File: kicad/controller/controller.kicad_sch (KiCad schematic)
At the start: 40 parts, among them J1 JST_BAT, J2 JST_BOOKMARK, J3 CONN_UPDI, J4 UART_DBG, Q1 DMP1045U, SW1 SW_DIP_x01, U1 DS3231, U2 TP4056, U3 ATTINY1616

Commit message: fix: fix wrong UPDI & DBG pin label
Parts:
- U4: value ~ -> (none)

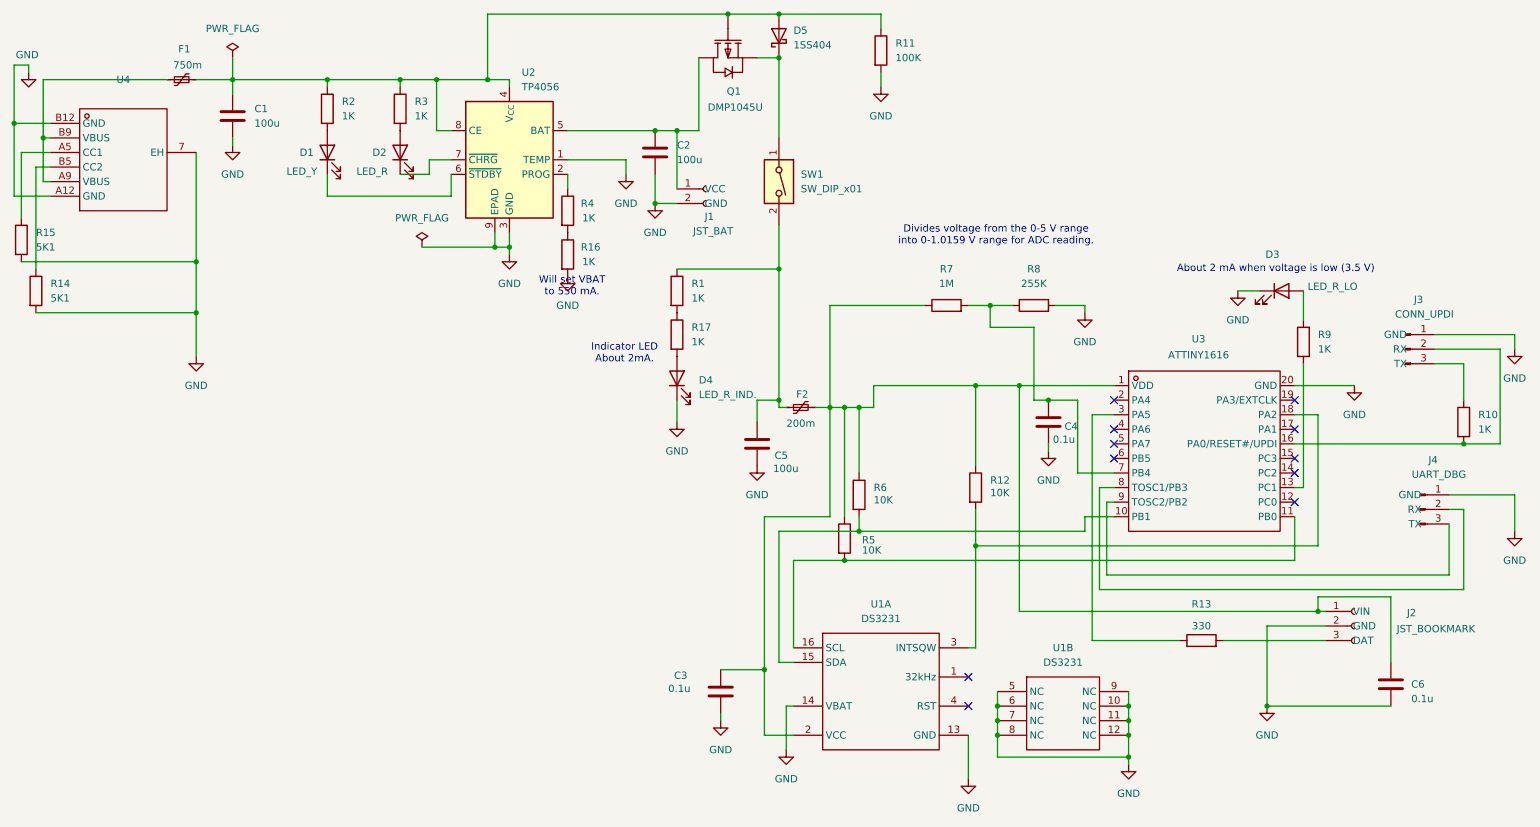
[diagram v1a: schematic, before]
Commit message: fix: make sense of the connection from power to peripherals make the DS3231 get power directly without a switch and add testing pads to connect power to MCU & LEDs in order to measure current.
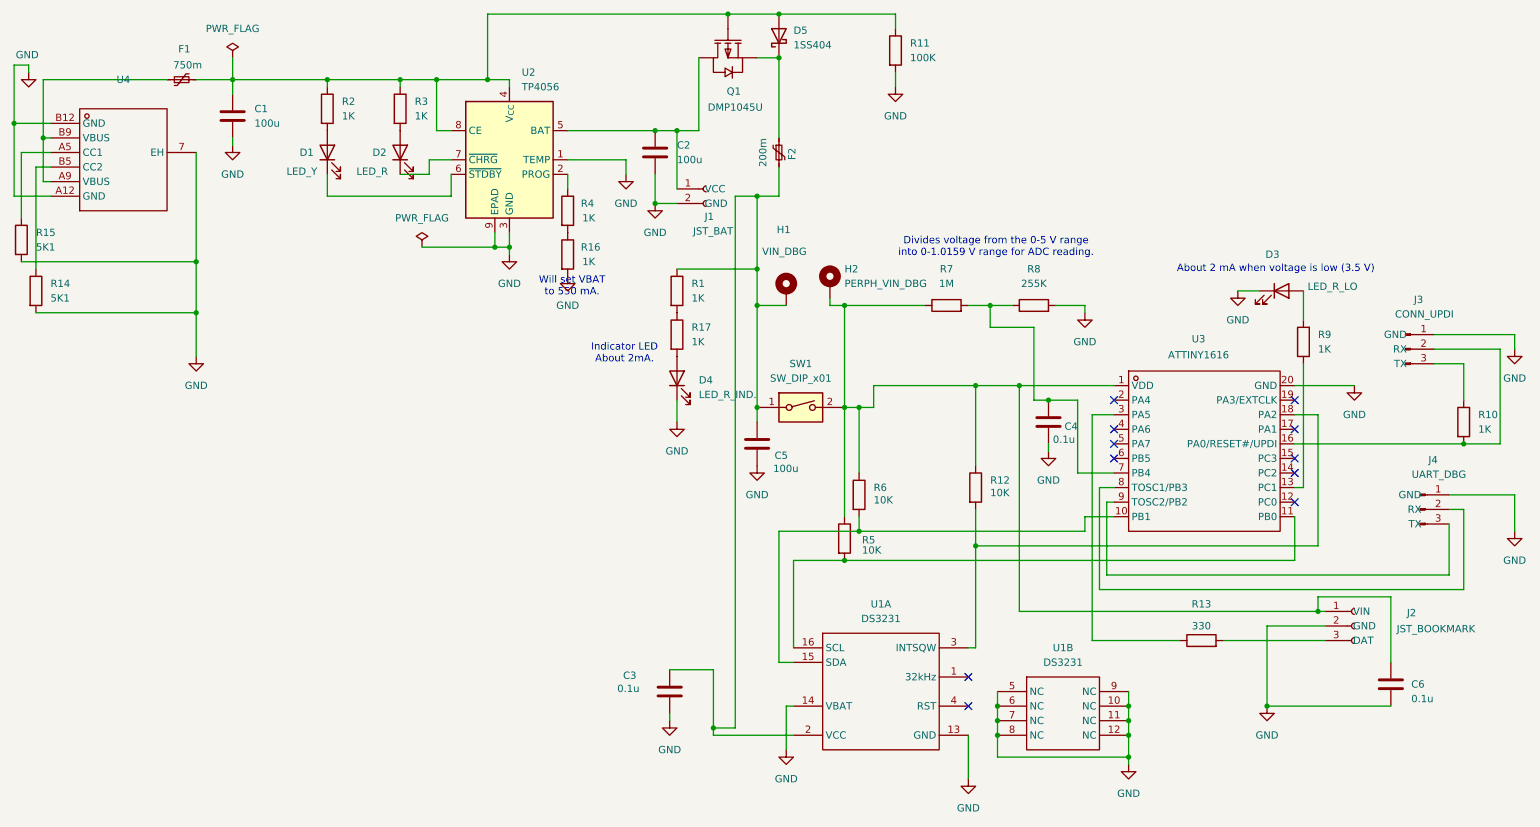
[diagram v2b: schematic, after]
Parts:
- added H1: VIN_DBG, Connector_Wire:SolderWirePad_1x01_SMD_1x2mm, symbol Mechanical:MountingHole_Pad
- added H2: PERPH_VIN_DBG, Connector_Wire:SolderWirePad_1x01_SMD_1x2mm, symbol Mechanical:MountingHole_Pad
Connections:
- net at C6.1, J2.1 (VIN), R12.1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: now also SW1.2, H2.1; no longer C3.1, F2.2, U1.2 (VCC)
- net at C5.1, R1.1: now also C3.1, F2.2, SW1.1, U1.2 (VCC), H1.1; no longer F2.1, SW1.2
- net at D5.1 (K), Q1.2 (S): now also F2.1; no longer SW1.1
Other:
- moved on the sheet: C3, F2, R11, SW1

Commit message: clean up position of footprints
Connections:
- net at C6.1, H2.1, J2.1 (VIN)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: now also R1.1
- net at C3.1, C5.1, F2.2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: no longer R1.1
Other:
- moved on the sheet: D4, R1, R17
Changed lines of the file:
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@@
 	(text "Indicator LED\nAbout 2mA."
 		(exclude_from_sim no)
-		(at 121.666 80.772 0)
+		(at 114.808 92.71 0)
 		(effects
 			(font
@@
 	)
 	(junction
-		(at 144.78 66.04)
-		(diameter 0)
-		(color 0 0 0 0)
-	)
-	(junction
 		(at 53.34 33.02)
 		(diameter 0)
@@
 	)
 	(junction
+		(at 160.02 80.01)
+		(diameter 0)
+		(color 0 0 0 0)
+	)
+	(junction
 		(at 144.78 90.17)
 		(diameter 0)
@@
 	(wire
 		(pts
+			(xy 123.19 80.01) (xy 123.19 83.82)
+		)
+		(stroke
+			(width 0)
+			(type default)
+		)
+	)
+	(wire
+		(pts
 			(xy 186.69 151.13) (xy 209.55 151.13)
 		)
@@
 	(wire
 		(pts
-			(xy 200.66 101.6) (xy 207.01 101.6)
+			(xy 160.02 80.01) (xy 160.02 90.17)
 		)
 		(stroke
@@
 	(wire
 		(pts
-			(xy 201.93 72.39) (xy 201.93 73.66)
+			(xy 200.66 101.6) (xy 207.01 101.6)
 		)
 		(stroke
@@
 	(wire
 		(pts
-			(xy 130.81 66.04) (xy 144.78 66.04)
+			(xy 201.93 72.39) (xy 201.93 73.66)
 		)
 		(stroke
@@
 	(wire
 		(pts
-			(xy 144.78 66.04) (xy 144.78 72.39)
+			(xy 144.78 53.34) (xy 144.78 72.39)
 		)
 		(stroke
@@
 	(wire
 		(pts
-			(xy 144.78 53.34) (xy 144.78 66.04)
-		)
-		(stroke
-			(width 0)
-			(type default)
-		)
-	)
-	(wire
-		(pts
 			(xy 17.78 30.48) (xy 17.78 31.75)
 		)
@@
 	(wire
 		(pts
-			(xy 130.81 88.9) (xy 130.81 92.71)
+			(xy 123.19 106.68) (xy 123.19 110.49)
 		)
 		(stroke
@@
 	(wire
 		(pts
+			(xy 160.02 80.01) (xy 123.19 80.01)
+		)
+		(stroke
+			(width 0)
+			(type default)
+		)
+	)
+	(wire
+		(pts
 			(xy 15.24 40.64) (xy 15.24 53.34)
 		)
@@
 	(wire
 		(pts
-			(xy 160.02 72.39) (xy 160.02 90.17)
+			(xy 160.02 72.39) (xy 160.02 80.01)
 		)
 		(stroke
@@
 	(symbol
 		(lib_id "Device:LED")
-		(at 130.81 85.09 90)
+		(at 123.19 102.87 90)
 		(unit 1)
 		(body_style 1)
@@
 		(fields_autoplaced yes)
 		(property "Reference" "D4"
-			(at 134.62 85.4074 90)
+			(at 127 103.1874 90)
 			(show_name no)
 			(do_not_autoplace no)
@@
 		)
 		(property "Value" "LED_R_IND."
-			(at 134.62 87.9474 90)
+			(at 127 105.7274 90)
 			(show_name no)
 			(do_not_autoplace no)
@@
 		)
 		(property "Footprint" "LED_THT:LED_D2.0mm_W4.8mm_H2.5mm_FlatTop"
-			(at 130.81 85.09 0)
+			(at 123.19 102.87 0)
 			(hide yes)
 			(show_name no)
@@
 		)
 		(property "Datasheet" ""
-			(at 130.81 85.09 0)
+			(at 123.19 102.87 0)
 			(hide yes)
 			(show_name no)
@@
 		)
 		(property "Description" "Light emitting diode"
-			(at 130.81 85.09 0)
+			(at 123.19 102.87 0)
 			(hide yes)
 			(show_name no)
@@
 		)
 		(property "Sim.Pins" "1=K 2=A"
-			(at 130.81 85.09 0)
+			(at 123.19 102.87 0)
 			(hide yes)
 			(show_name no)
@@
 	(symbol
 		(lib_id "Device:R")
-		(at 130.81 69.85 0)
+		(at 123.19 87.63 0)
 		(unit 1)
 		(body_style 1)
@@
 		(fields_autoplaced yes)
 		(property "Reference" "R1"
-			(at 133.35 68.5799 0)
+			(at 125.73 86.3599 0)
 			(show_name no)
 			(do_not_autoplace no)
@@
 		)
 		(property "Value" "1K"
-			(at 133.35 71.1199 0)
+			(at 125.73 88.8999 0)
 			(show_name no)
 			(do_not_autoplace no)
@@
 		)
 		(property "Footprint" "Resistor_SMD:R_0603_1608Metric"
-			(at 129.032 69.85 90)
+			(at 121.412 87.63 90)
 			(hide yes)
 			(show_name no)
@@
 		)
 		(property "Datasheet" ""
-			(at 130.81 69.85 0)
+			(at 123.19 87.63 0)
 			(hide yes)
 			(show_name no)
@@
 		)
 		(property "Description" "Resistor"
-			(at 130.81 69.85 0)
+			(at 123.19 87.63 0)
 			(hide yes)
 			(show_name no)
@@
 	(symbol
 		(lib_id "Device:R")
-		(at 130.81 77.47 0)
+		(at 123.19 95.25 0)
 		(unit 1)
 		(body_style 1)
@@
 		(fields_autoplaced yes)
 		(property "Reference" "R17"
-			(at 133.35 76.1999 0)
+			(at 125.73 93.9799 0)
 			(show_name no)
 			(do_not_autoplace no)
@@
 		)
 		(property "Value" "1K"
-			(at 133.35 78.7399 0)
+			(at 125.73 96.5199 0)
 			(show_name no)
 			(do_not_autoplace no)
@@
 		)
 		(property "Footprint" "Resistor_SMD:R_0603_1608Metric"
-			(at 129.032 77.47 90)
+			(at 121.412 95.25 90)
 			(hide yes)
 			(show_name no)
@@
 		)
 		(property "Datasheet" ""
-			(at 130.81 77.47 0)
+			(at 123.19 95.25 0)
 			(hide yes)
 			(show_name no)
@@
 		)
 		(property "Description" "Resistor"
-			(at 130.81 77.47 0)
+			(at 123.19 95.25 0)
 			(hide yes)
 			(show_name no)
@@
 	(symbol
 		(lib_id "power:GND")
-		(at 130.81 92.71 0)
+		(at 123.19 110.49 0)
 		(unit 1)
 		(body_style 1)
@@
 		(fields_autoplaced yes)
 		(property "Reference" "#PWR019"
-			(at 130.81 99.06 0)
+			(at 123.19 116.84 0)
 			(hide yes)
 			(show_name no)
@@
 		)
 		(property "Value" "GND"
-			(at 130.81 97.79 0)
+			(at 123.19 115.57 0)
 			(show_name no)
 			(do_not_autoplace no)
@@
 		)
 		(property "Footprint" ""
-			(at 130.81 92.71 0)
+			(at 123.19 110.49 0)
 			(hide yes)
 			(show_name no)
@@
 		)
 		(property "Datasheet" ""
-			(at 130.81 92.71 0)
+			(at 123.19 110.49 0)
 			(hide yes)
 			(show_name no)
@@
 		)
 		(property "Description" "Power symbol creates a global label with name \"GND\" , ground"
-			(at 130.81 92.71 0)
+			(at 123.19 110.49 0)
 			(hide yes)
 			(show_name no)

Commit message: change usb C footprint to USB-TYPE-C-006 https://jlcpcb.com/partdetail/DEALON-USB_TYPE_C006/C2927026
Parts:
- U4: footprint custom-footprints:TYPE-C-SMD_TYPE-C-6P -> custom-footprints:USB-C-SMD_USB-TYPE-C-006; symbol Misc_Components:USB-TYPE-C-009 -> Misc_Components:USB-TYPE-C-006; Manufacturer Part USB-TYPE-C-009 -> USB-TYPE-C-006; Supplier Part C2927029 -> C2927026
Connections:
- net GND: now also U4.1 (SHELL), U4.2 (SHELL), U4.3 (SHELL), U4.4 (SHELL); no longer U4.7 (EH)
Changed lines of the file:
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@@
+	)
+	(junction
+		(at 15.24 41.91)
+		(diameter 0)
+		(color 0 0 0 0)
 	)
 	(junction
@@
 	)
 	(junction
+		(at 20.32 44.45)
+		(diameter 0)
+		(color 0 0 0 0)
+	)
+	(junction
 		(at 242.57 125.73)
 		(diameter 0)
@@
 	)
 	(junction
-		(at 20.32 43.18)
+		(at 46.99 52.07)
 		(diameter 0)
 		(color 0 0 0 0)
@@
 	)
 	(junction
+		(at 46.99 54.61)
+		(diameter 0)
+		(color 0 0 0 0)
+	)
+	(junction
 		(at 162.56 111.76)
 		(diameter 0)
@@
 	)
 	(junction
-		(at 15.24 40.64)
-		(diameter 0)
-		(color 0 0 0 0)
-	)
-	(junction
 		(at 53.34 33.02)
 		(diameter 0)
@@
 	(junction
 		(at 46.99 73.66)
+		(diameter 0)
+		(color 0 0 0 0)
+	)
+	(junction
+		(at 46.99 44.45)
 		(diameter 0)
 		(color 0 0 0 0)
@@
 	(wire
 		(pts
+			(xy 45.72 54.61) (xy 46.99 54.61)
+		)
+		(stroke
+			(width 0)
+			(type default)
+		)
+	)
+	(wire
+		(pts
 			(xy 238.506 91.44) (xy 242.57 91.44)
 		)
@@
 	(wire
 		(pts
-			(xy 19.05 48.26) (xy 21.59 48.26)
-		)
-		(stroke
-			(width 0)
-			(type default)
-		)
-	)
-	(wire
-		(pts
 			(xy 121.92 46.99) (xy 121.92 49.53)
 		)
@@
 	(wire
 		(pts
+			(xy 46.99 54.61) (xy 46.99 64.77)
+		)
+		(stroke
+			(width 0)
+			(type default)
+		)
+	)
+	(wire
+		(pts
 			(xy 195.58 96.52) (xy 195.58 97.79)
 		)
@@
 	(wire
 		(pts
+			(xy 46.99 44.45) (xy 46.99 52.07)
+		)
+		(stroke
+			(width 0)
+			(type default)
+		)
+	)
+	(wire
+		(pts
 			(xy 265.43 110.49) (xy 265.43 119.38)
 		)
@@
 	(wire
 		(pts
-			(xy 16.51 45.72) (xy 16.51 57.15)
+			(xy 16.51 54.61) (xy 16.51 57.15)
 		)
 		(stroke
@@
 	(wire
 		(pts
-			(xy 20.32 50.8) (xy 21.59 50.8)
+			(xy 20.32 52.07) (xy 22.86 52.07)
 		)
 		(stroke
@@
 	(wire
 		(pts
-			(xy 20.32 33.02) (xy 20.32 43.18)
+			(xy 20.32 33.02) (xy 20.32 44.45)
 		)
 		(stroke
@@
 	(wire
 		(pts
+			(xy 15.24 41.91) (xy 22.86 41.91)
+		)
+		(stroke
+			(width 0)
+			(type default)
+		)
+	)
+	(wire
+		(pts
 			(xy 160.02 90.17) (xy 160.02 109.22)
 		)
@@
 	(wire
 		(pts
+			(xy 15.24 41.91) (xy 15.24 49.53)
+		)
+		(stroke
+			(width 0)
+			(type default)
+		)
+	)
+	(wire
+		(pts
 			(xy 203.2 91.44) (xy 203.2 130.81)
 		)
@@
 	(wire
 		(pts
+			(xy 19.05 46.99) (xy 22.86 46.99)
+		)
+		(stroke
+			(width 0)
+			(type default)
+		)
+	)
+	(wire
+		(pts
 			(xy 88.9 33.02) (xy 97.79 33.02)
 		)
@@
 	(wire
 		(pts
+			(xy 45.72 52.07) (xy 46.99 52.07)
+		)
+		(stroke
+			(width 0)
+			(type default)
+		)
+	)
+	(wire
+		(pts
 			(xy 139.7 21.59) (xy 148.59 21.59)
 		)
@@
 	(wire
 		(pts
-			(xy 16.51 45.72) (xy 21.59 45.72)
+			(xy 16.51 54.61) (xy 22.86 54.61)
 		)
 		(stroke
@@
 	(wire
 		(pts
+			(xy 45.72 44.45) (xy 46.99 44.45)
+		)
+		(stroke
+			(width 0)
+			(type default)
+		)
+	)
+	(wire
+		(pts
+			(xy 46.99 41.91) (xy 46.99 44.45)
+		)
+		(stroke
+			(width 0)
+			(type default)
+		)
+	)
+	(wire
+		(pts
+			(xy 46.99 52.07) (xy 46.99 54.61)
+		)
+		(stroke
+			(width 0)
+			(type default)
+		)
+	)
+	(wire
+		(pts
 			(xy 15.24 30.48) (xy 17.78 30.48)
 		)
@@
 	(wire
 		(pts
-			(xy 15.24 53.34) (xy 21.59 53.34)
+			(xy 15.24 49.53) (xy 22.86 49.53)
 		)
 		(stroke
@@
 	(wire
 		(pts
-			(xy 15.24 30.48) (xy 15.24 40.64)
+			(xy 15.24 30.48) (xy 15.24 41.91)
 		)
 		(stroke
@@
 	(wire
 		(pts
-			(xy 20.32 43.18) (xy 21.59 43.18)
+			(xy 20.32 44.45) (xy 22.86 44.45)
 		)
 		(stroke
@@
 	(wire
 		(pts
+			(xy 45.72 41.91) (xy 46.99 41.91)
+		)
+		(stroke
+			(width 0)
+			(type default)
+		)
+	)
+	(wire
+		(pts
 			(xy 101.6 33.02) (xy 101.6 34.29)
 		)
@@
 	(wire
 		(pts
+			(xy 19.05 46.99) (xy 19.05 66.04)
+		)
+		(stroke
+			(width 0)
+			(type default)
+		)
+	)
+	(wire
+		(pts
 			(xy 201.93 109.22) (xy 201.93 111.76)
 		)
@@
 	(wire
 		(pts
-			(xy 15.24 40.64) (xy 15.24 53.34)
-		)
-		(stroke
-			(width 0)
-			(type default)
-		)
-	)
-	(wire
-		(pts
 			(xy 129.54 143.51) (xy 129.54 144.78)
 		)
@@
 	(wire
 		(pts
-			(xy 46.99 45.72) (xy 46.99 64.77)
-		)
-		(stroke
-			(width 0)
-			(type default)
-		)
-	)
-	(wire
-		(pts
 			(xy 69.85 33.02) (xy 82.55 33.02)
 		)
@@
 	(wire
 		(pts
-			(xy 20.32 43.18) (xy 20.32 50.8)
+			(xy 20.32 44.45) (xy 20.32 52.07)
 		)
 		(stroke
@@
 	(wire
 		(pts
-			(xy 15.24 40.64) (xy 21.59 40.64)
-		)
-		(stroke
-			(width 0)
-			(type default)
-		)
-	)
-	(wire
-		(pts
 			(xy 160.02 72.39) (xy 160.02 80.01)
 		)
@@
 		(pts
 			(xy 129.54 135.89) (xy 137.16 135.89)
-		)
-		(stroke
-			(width 0)
-			(type default)
-		)
-	)
-	(wire
-		(pts
-			(xy 19.05 48.26) (xy 19.05 66.04)
 		)
 		(stroke
@@
 	)
 	(symbol
-		(lib_id "Misc_Components:USB-TYPE-C-009")
+		(lib_id "Misc_Components:USB-TYPE-C-006")
 		(at 34.29 48.26 0)
 		(unit 1)
@@
 		(fields_autoplaced yes)
 		(property "Reference" "U4"
-			(at 34.29 33.02 0)
+			(at 34.29 36.83 0)
 			(show_name no)
 			(do_not_autoplace no)
@@
 			)
 		)
-		(property "Footprint" "custom-footprints:TYPE-C-SMD_TYPE-C-6P"
+		(property "Footprint" "custom-footprints:USB-C-SMD_USB-TYPE-C-006"
 			(at 34.29 48.26 0)
 			(hide yes)
@@
 			)
 		)
-		(property "Datasheet" "https://item.szlcsc.com/datasheet/USB-TYPE-C-009/3252498.html"
+		(property "Datasheet" "https://item.szlcsc.com/datasheet/USB-TYPE-C-006/3252495.html"
 			(at 34.29 48.26 0)
 			(hide yes)
@@
 			)
 		)
-		(property "Manufacturer Part" "USB-TYPE-C-009"
+		(property "Manufacturer Part" "USB-TYPE-C-006"
 			(at 34.29 48.26 0)
 			(hide yes)
@@
 			)
 		)
-		(property "Supplier Part" "C2927029"
+		(property "Supplier Part" "C2927026"
 			(at 34.29 48.26 0)
 			(hide yes)
@@
 		(pin "A9"
 		)
-		(pin "7"
+		(pin "2"
 		)
 		(pin "A12"
 		)
+		(pin "1"
+		)
+		(pin "4"
+		)
+		(pin "3"
+		)
 		(instances

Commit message: replace out of stock resistors with fresh ones * swap 1M+255K voltage divider to 787K+200K * swap 330 to 330 but less power rating the entire bom is now $0.1 cheaper!
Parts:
- R7: value 1M -> 787K
- R8: value 255K -> 200K
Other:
- note added: "Divides voltage from the 0-5 V range into 0-1.013 V range for ADC reading."
- note removed: "Divides voltage from the 0-5 V range into 0-1.0159 V range for ADC reading."
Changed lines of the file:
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@@
 		)
 	)
-	(text "Divides voltage from the 0-5 V range\ninto 0-1.0159 V range for ADC reading."
+	(text "Divides voltage from the 0-5 V range\ninto 0-1.013 V range for ADC reading."
 		(exclude_from_sim no)
 		(at 186.436 62.23 0)
@@
 			)
 		)
-		(property "Value" "255K"
+		(property "Value" "200K"
 			(at 193.04 68.58 90)
 			(show_name no)
@@
 			)
 		)
-		(property "Value" "1M"
+		(property "Value" "787K"
 			(at 177.8 68.58 90)
 			(show_name no)
